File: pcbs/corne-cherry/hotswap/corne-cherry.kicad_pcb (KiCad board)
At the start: 2 copper layers, 277.2 x 107.5 mm, 190 parts, among them J1 TYPE-C-31-M-13C, J2 TRS, J3 Conn_01x04, J4 Conn_01x03, SW1 SW_Push, SW10 SW_Push, SW11 SW_Push, SW12 SW_Push, SW13 SW_Push, SW14 SW_Push, SW15 SW_Push, SW16 SW_Push, SW17 SW_Push, SW18 SW_Push, SW19 SW_Push, SW2 SW_Push, SW20 SW_Push, SW21 SW_Push, SW22 SW_Push, SW23 SW_Push, SW24 SW_Push, SW3 SW_Push, SW4 SW_Push, SW5 SW_Push, SW6 SW_Push, SW7 SW_Push, SW8 SW_Push, SW9 SW_Push, U1 RP2040, U2 NCP1117LPST33T3G, U3 TPD4E05U06DQAR, U4 W25Q128JVSIQ, Y1 12MHz 18pF

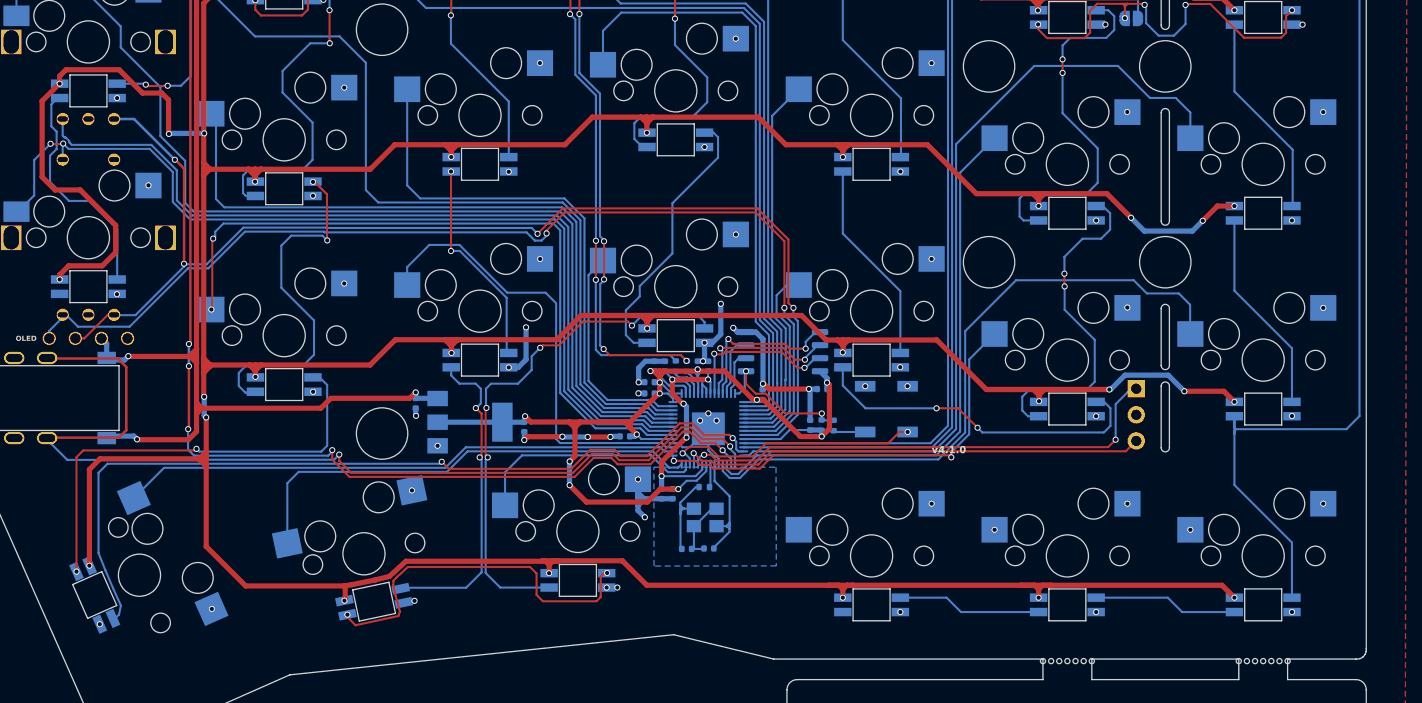
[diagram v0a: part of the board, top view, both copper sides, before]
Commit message: add right keys wiring
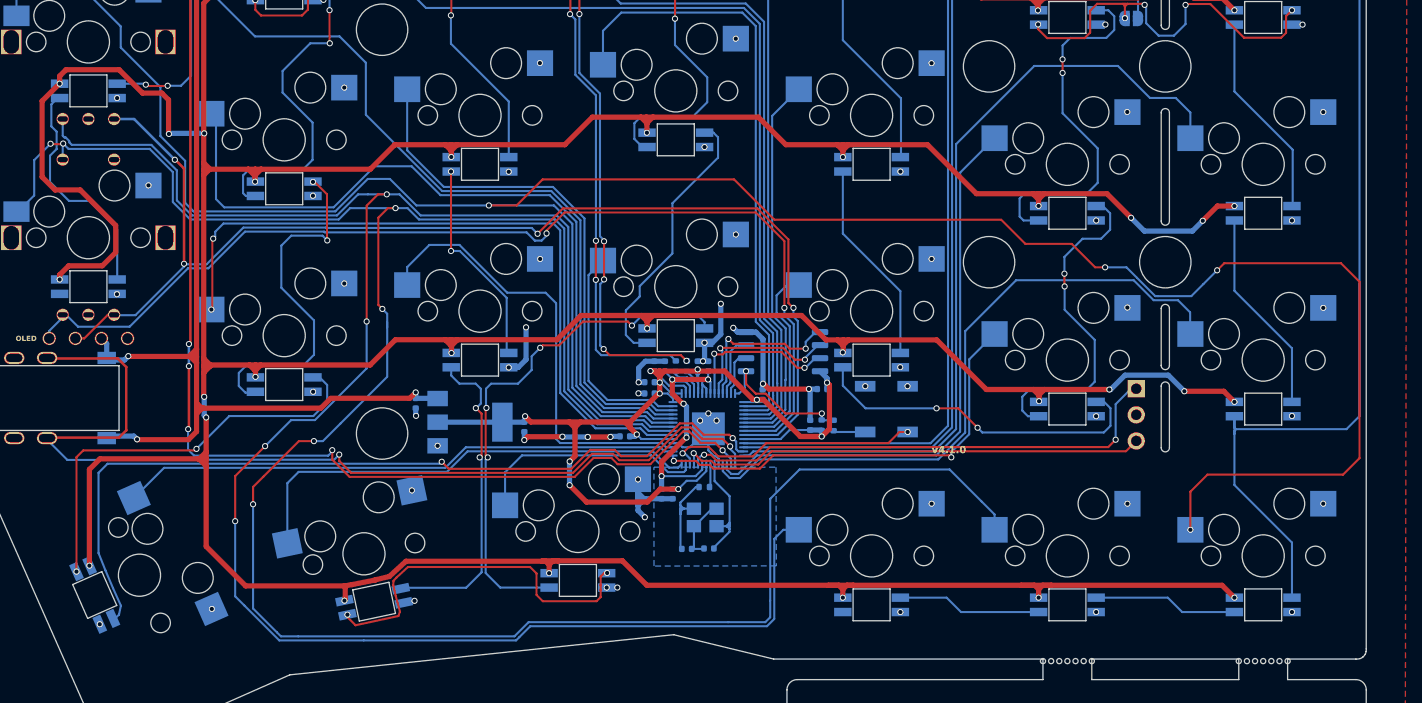
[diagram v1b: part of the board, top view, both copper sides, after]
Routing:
- net /right/KEY23: track 92.8 -> 231.5 mm, vias 3 -> 6
- net /right/KEY22: track 102.6 -> 236.4 mm, vias 1 -> 4
- net /right/KEY24: track 83.8 -> 198.2 mm, vias 0 -> 4
- net /right/KEY4: track 85.9 -> 81.6 mm
- net /right/KEY3: track 70.5 -> 73.8 mm
- net Net-(rLED1-DOUT): track 43.3 -> 40.6 mm
- net /right/KEY6: track 53.6 -> 51.6 mm
